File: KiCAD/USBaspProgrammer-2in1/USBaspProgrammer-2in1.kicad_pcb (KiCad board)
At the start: 2 copper layers, 73.7 x 31.8 mm, 22 parts, among them J1 USB_B, J2 ISP_header_Conn_02x05_Odd_Even, U1 ATmega88-20PU, Y1 12MHz

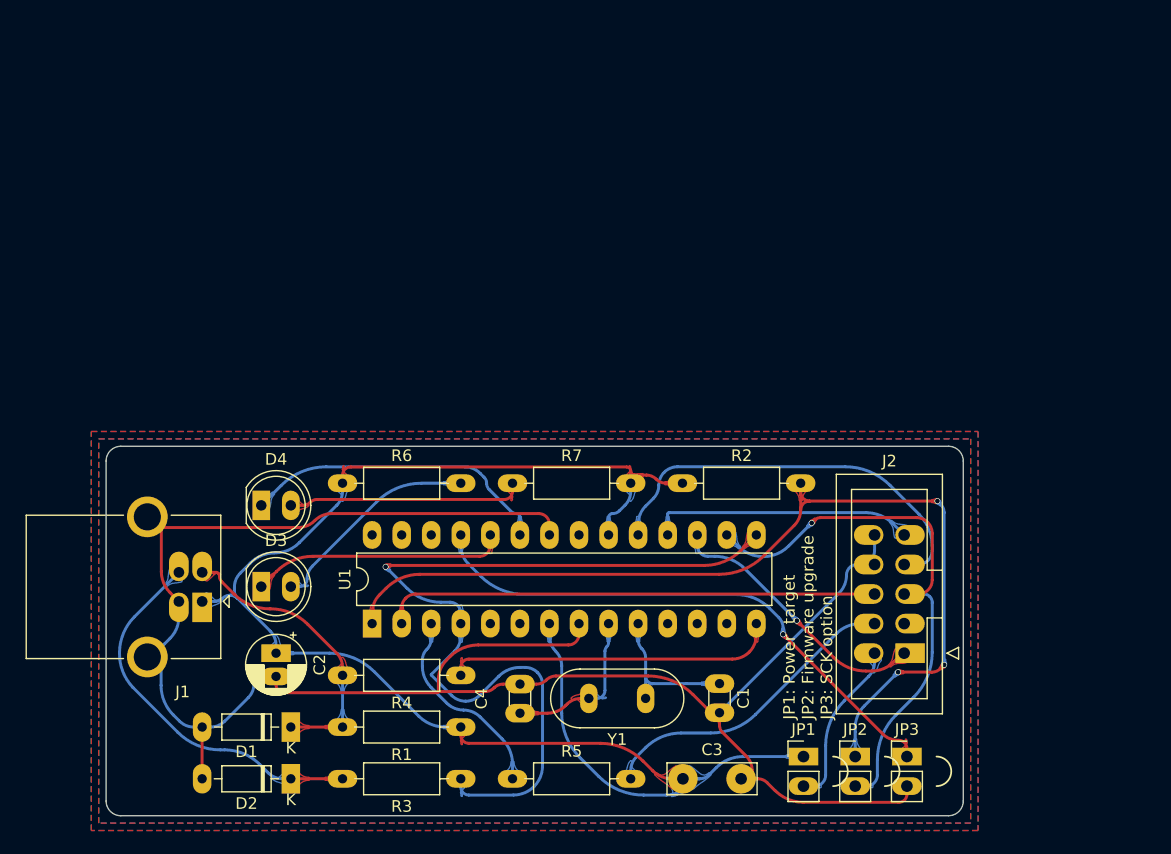
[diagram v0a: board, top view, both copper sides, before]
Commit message: schematics and pcb
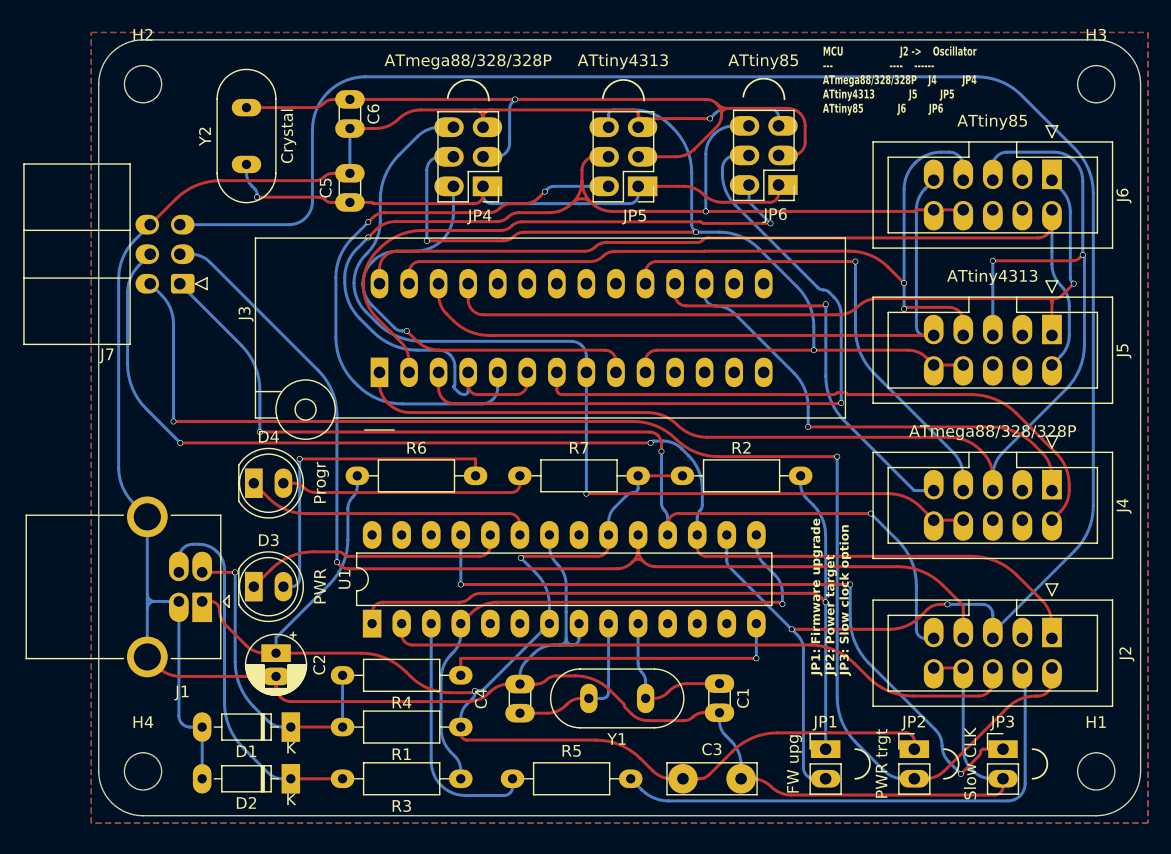
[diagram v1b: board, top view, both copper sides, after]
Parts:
- added C5: 22p, My_Misc:C_Disc_D3.0mm_W1.6mm_P2.50mm_larg, F.Cu at (135.9, 76.2)
- added C6: 22p, My_Misc:C_Disc_D3.0mm_W1.6mm_P2.50mm_larg, F.Cu at (135.9, 67.3)
- added H1: MountingHole, MountingHole:MountingHole_3.2mm_M3, F.Cu at (200.0, 125.1)
- added H2: MountingHole, MountingHole:MountingHole_3.2mm_M3, F.Cu at (118.1, 66.0)
- added H3: MountingHole, MountingHole:MountingHole_3.2mm_M3, F.Cu at (200.0, 66.0)
- added H4: MountingHole, MountingHole:MountingHole_3.2mm_M3, F.Cu at (118.1, 125.1)
- added J3: ZIF Socket, My_Misc:ZIF_DIP_Socket-28_W6.9_W7.62_W7.62_W12.7_W13.5_large, F.Cu at (138.4, 90.8)
- added J4: ATmega88/328/328P, My_Misc:IDC-Header_2x05_P2.54mm_Vertical_large, F.Cu at (196.2, 101.0)
- added J5: ATtiny4313, My_Misc:IDC-Header_2x05_P2.54mm_Vertical_large, F.Cu at (196.2, 87.6)
- added J6: ATtiny85, My_Misc:IDC-Header_2x05_P2.54mm_Vertical_large, F.Cu at (196.2, 74.3)
- added J7: ISP_header_Conn_02x03_Odd_Even, My_Misc:IDC-Header_2x03_P2.54mm_Horizontal_large, F.Cu at (121.3, 83.2)
- added JP4: ATmega88/328/328P, My_Parts:3-pole_jumper_2x03_P2.54mm_Vertical, F.Cu at (147.3, 74.8)
- added JP5: ATtiny4313, My_Parts:3-pole_jumper_2x03_P2.54mm_Vertical, F.Cu at (160.7, 74.8)
- added JP6: ATtiny85, My_Parts:3-pole_jumper_2x03_P2.54mm_Vertical, F.Cu at (172.7, 74.7)
- added Y2: Crystal, My_Misc:Crystal_HC49-4H_Vertical_large, F.Cu at (127.0, 72.9)
- D3: value LED green -> PWR
- D4: value LED red -> Progr
- JP1: renamed from JP2; value Self programming -> FW upg
- JP2: renamed from JP1; value Supply target -> PWR trgt
- JP3: value Slow SCK -> Slow CLK
- R1, R2, R3, R4, R5, R6, R7: footprint My_Misc:R_Axial_DIN0207_L6.3mm_D2.5mm_P10.16mm_Horizontal_larger_pads -> My_Misc:R_Axial_DIN0207_L6.3mm_D2.5mm_P10.16mm_Horizontal_large
- moved J2 12.8 mm to (196.2, 113.7), turned to -90 degrees
- moved JP2 9.55 mm to (184.4, 123.2)
- moved JP3 8.28 mm to (192.0, 123.2)
- moved JP1 2.62 mm to (176.8, 123.2)
- moved D4 2.01 mm to (127.6, 100.3)
- moved R6 1.42 mm to (136.5, 99.7)
- moved R7 0.90 mm to (150.5, 99.7)
- moved D3 0.64 mm to (127.6, 109.2)
- moved R2 0.64 mm to (164.5, 99.7)
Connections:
- net XTAL1 renamed Prog-XTAL1
- net XTAL2 renamed Prog-XTAL2
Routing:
- net Net-(J2-RST): track 48.8 -> 179.7 mm, vias 1 -> 2
- net 1: track 0.00 -> 113.3 mm, vias 0 -> 2
- net Net-(J2-VCC): track 14.3 -> 117.8 mm, vias 0 -> 2
- net 4: track 0.00 -> 101.2 mm, vias 0 -> 2
- net 10: track 0.00 -> 94.4 mm, vias 0 -> 3
- net 8: track 0.00 -> 85.7 mm, vias 0 -> 1
- net Net-(J2-MOSI): track 23.4 -> 105.7 mm, vias 1 -> 2
- net 28: track 0.00 -> 76.3 mm
- net 27: track 0.00 -> 71.1 mm, vias 0 -> 2
- net XTAL2: track 0.00 -> 71.1 mm, vias 0 -> 1
- net GND: track 174.5 -> 243.5 mm, vias 0 -> 1
- net 25: track 0.00 -> 68.3 mm, vias 0 -> 1
- net Net-(J2-MISO): track 22.8 -> 90.5 mm, vias 0 -> 3
- net 3: track 0.00 -> 64.0 mm, vias 0 -> 1
- net 26: track 0.00 -> 60.2 mm
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- removed copper zone on B.Cu, net (none)
- removed copper zone on F.Cu, net (none)
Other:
- board size 73.7 x 31.8 mm -> 89.5 x 66.7 mm
- board text added: "JP1: Firmware upgrade JP2: Power target JP3: Slow clock option"
- board text added: "MCU J2 -> Oscillator --- ---- ------ ATmega88/328/328P J4 JP4 ATtiny4313 J5 JP5 ATtiny85 J6 JP6"
- board text added: "USBaspProgrammer-2in1 github.com/jonsag/USBaspProgrammer"
- board text removed: "JP1: Power target JP2: Firmware upgrade JP3: SCK option"
- board text removed: "USBaspProgrammer Design: Jon Sagebrand jonsagebrand@gmail.com"

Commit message: pcb
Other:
- board text added: "USBaspProgrammer-2in1"
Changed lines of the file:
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@@
+		)
+	)
+	(gr_text "USBaspProgrammer-2in1"
+		(at 125.095 100.965 90)
+		(layer "F.SilkS")
+		(effects
+			(font
+				(size 1 1)
+				(thickness 0.15)
+			)
+			(justify left bottom)
 		)
 	)
